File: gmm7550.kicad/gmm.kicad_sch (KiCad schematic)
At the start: 6 parts

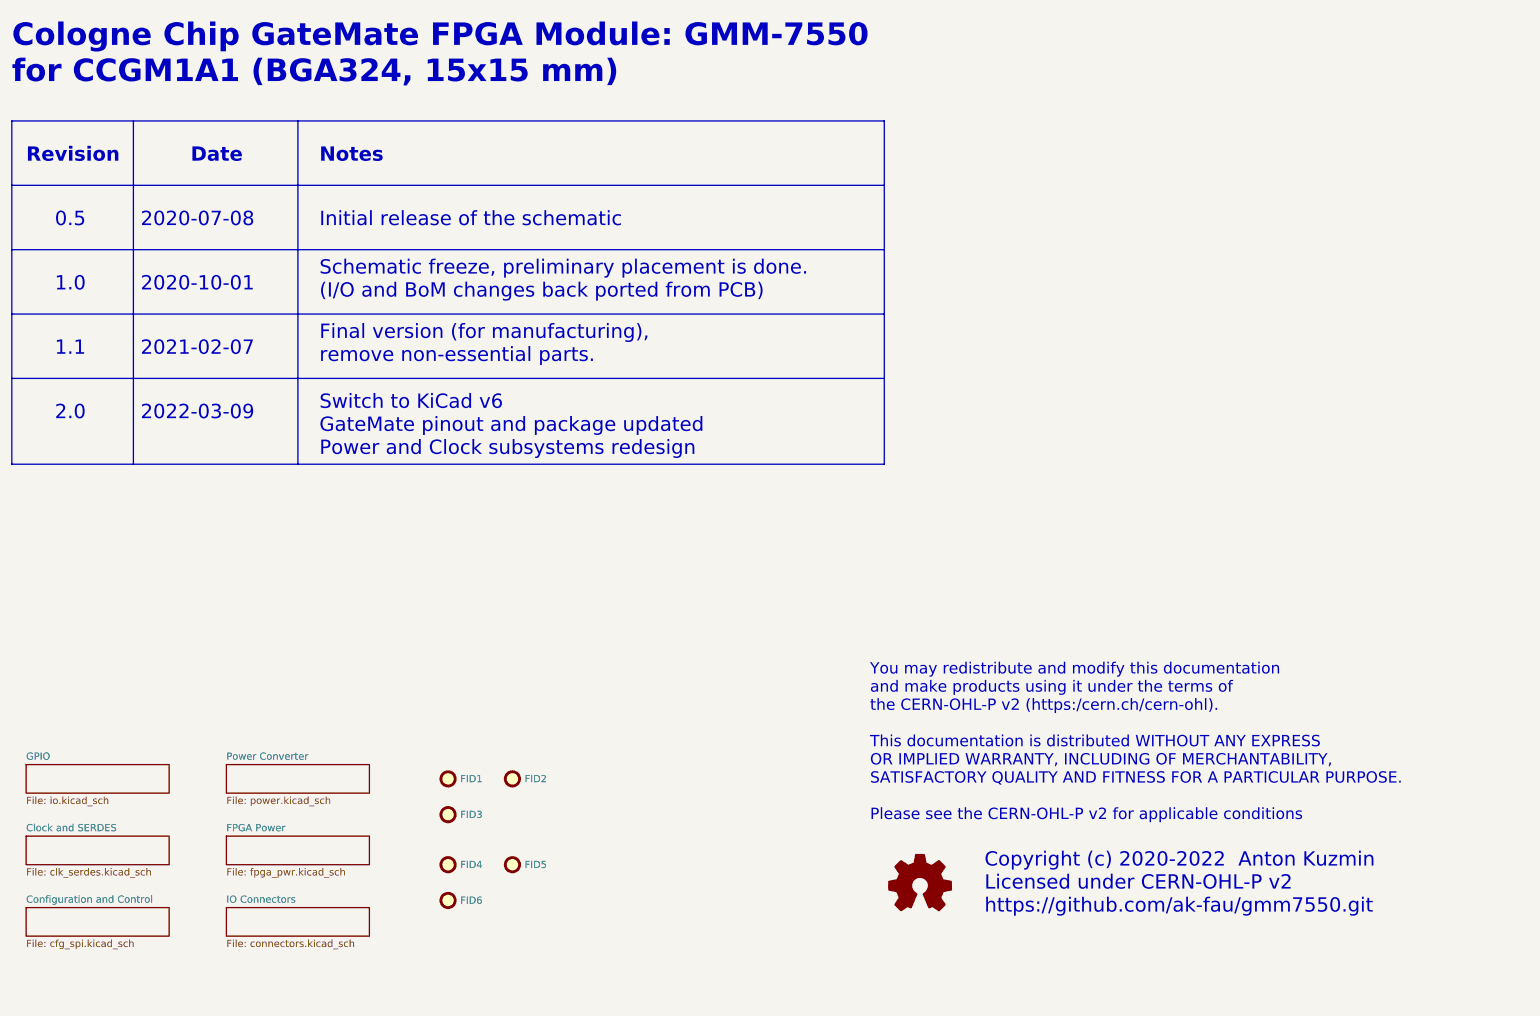
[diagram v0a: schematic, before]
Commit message: Change U7 footprint due to the part availability, revision and date are updated, DRC warnings clean-up (GMM-7550)
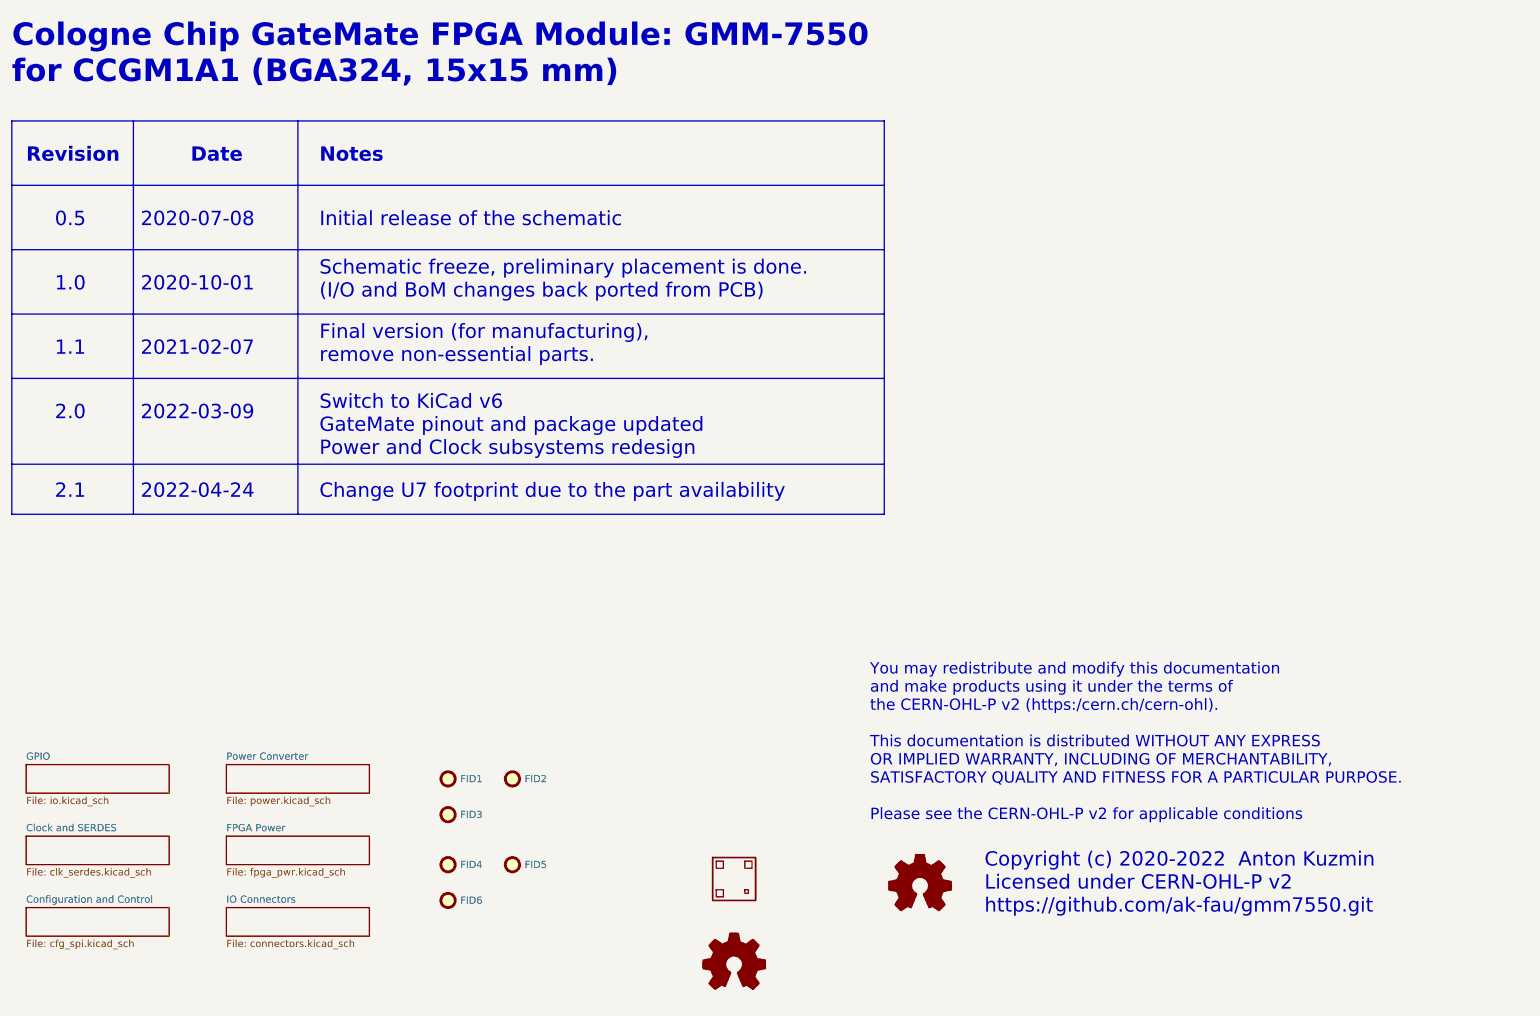
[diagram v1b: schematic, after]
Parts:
- added LOGO1: (no value), symbol Graphic:Logo_Open_Hardware_Small
- added QR1: (no value), gmm:GitHub_link_QR, symbol gmm_v6:GitHub_link_QR
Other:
- note added: "2.1"
- note added: "2022-04-24"
- note added: "Change U7 footprint due to the part availability"
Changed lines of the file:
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@@
   (title_block
     (title "GateMate FPGA Module: GMM-7550")
-    (date "2022-03-09")
-    (rev "2.0")
+    (date "2022-04-24")
+    (rev "2.1")
   )
   (polyline (pts (xy 25.4 72.39) (xy 180.34 72.39))
     (stroke (width 0.2032) (type solid) (color 0 0 0 0))
   )
+  (polyline (pts (xy 25.4 99.06) (xy 180.34 99.06))
+    (stroke (width 0.2032) (type solid) (color 0 0 0 0))
+  )
   (polyline (pts (xy 25.4 83.82) (xy 180.34 83.82))
     (stroke (width 0.2032) (type solid) (color 0 0 0 0))
   )
-  (polyline (pts (xy 180.34 38.1) (xy 180.34 99.06))
+  (polyline (pts (xy 180.34 38.1) (xy 180.34 107.95))
     (stroke (width 0.2032) (type solid) (color 0 0 0 0))
   )
-  (polyline (pts (xy 46.99 38.1) (xy 46.99 99.06))
+  (polyline (pts (xy 46.99 38.1) (xy 46.99 107.95))
     (stroke (width 0.2032) (type solid) (color 0 0 0 0))
   )
@@
     (stroke (width 0.2032) (type solid) (color 0 0 0 0))
   )
-  (polyline (pts (xy 76.2 38.1) (xy 76.2 99.06))
+  (polyline (pts (xy 76.2 38.1) (xy 76.2 107.95))
     (stroke (width 0.2032) (type solid) (color 0 0 0 0))
   )
@@
     (stroke (width 0.2032) (type solid) (color 0 0 0 0))
   )
-  (polyline (pts (xy 25.4 38.1) (xy 25.4 99.06))
+  (polyline (pts (xy 25.4 38.1) (xy 25.4 107.95))
     (stroke (width 0.2032) (type solid) (color 0 0 0 0))
   )
-  (polyline (pts (xy 25.4 99.06) (xy 180.34 99.06))
+  (polyline (pts (xy 25.4 107.95) (xy 180.34 107.95))
     (stroke (width 0.2032) (type solid) (color 0 0 0 0))
   )
@@
   (text "Final version (for manufacturing),\nremove non-essential parts."
     (at 80.01 81.28 0)
+    (effects (font (size 2.54 2.54)) (justify left bottom))
+  )
+  (text "2022-04-24" (at 48.26 105.41 0)
     (effects (font (size 2.54 2.54)) (justify left bottom))
   )
@@
     (effects (font (size 2.54 2.54)) (justify left bottom))
   )
+  (text "Change U7 footprint due to the part availability" (at 80.01 105.41 0)
+    (effects (font (size 2.54 2.54)) (justify left bottom))
+  )
   (text "Cologne Chip GateMate FPGA Module: GMM-7550\nfor CCGM1A1 (BGA324, 15x15 mm)"
     (at 25.4 31.75 0)
     (effects (font (size 3.9878 3.9878) (thickness 0.7976) bold) (justify left bottom))
+  )
+  (text "2.1" (at 33.02 105.41 0)
+    (effects (font (size 2.54 2.54)) (justify left bottom))
   )
   (text "2.0" (at 33.02 91.44 0)
@@
     )
     (property "Datasheet" "~" (id 3) (at 186.69 173.99 0)
+      (effects (font (size 1.27 1.27)) hide)
+    )
+  )
+  (symbol (lib_id "gmm_v6:GitHub_link_QR") (at 153.67 172.72 0) (unit 1)
+    (in_bom no) (on_board yes)
+    (property "Reference" "QR1" (id 0) (at 153.67 172.72 0)
+      (effects (font (size 1.27 1.27)) hide)
+    )
+    (property "Value" "" (id 1) (at 147.32 177.8 0)
+      (effects (font (size 1.27 1.27)) (justify left))
+    )
+    (property "Footprint" "gmm:GitHub_link_QR" (id 2) (at 153.67 172.72 0)
+      (effects (font (size 1.27 1.27)) hide)
+    )
+    (property "Datasheet" "" (id 3) (at 153.67 172.72 0)
+      (effects (font (size 1.27 1.27)) hide)
+    )
+  )
+  (symbol (lib_name "Logo_Open_Hardware_Small_1") (lib_id "Graphic:Logo_Open_Hardware_Small") (at 153.67 187.96 0) (unit 1)
+    (in_bom no) (on_board yes) (fields_autoplaced)
+    (property "Reference" "LOGO1" (id 0) (at 153.67 180.975 0)
+      (effects (font (size 1.27 1.27)) hide)
+    )
+    (property "Value" "" (id 1) (at 153.67 193.675 0))
+    (property "Footprint" "" (id 2) (at 153.67 187.96 0)
+      (effects (font (size 1.27 1.27)) hide)
+    )
+    (property "Datasheet" "~" (id 3) (at 153.67 187.96 0)
       (effects (font (size 1.27 1.27)) hide)
     )
@@
       (reference "L10") (unit 1) (value "ASPIAIG-FLR4020-1R0M-T") (footprint "gmm:L_Abracon_F4020_4.1x4.1mm")
     )
+    (path "/2df1f7fd-f252-4599-b779-f9b4ea84bccf"
+      (reference "LOGO1") (unit 1) (value "Logo_Open_Hardware_Small") (footprint "Symbol:OSHW-Logo2_7.3x6mm_SilkScreen")
+    )
     (path "/00000000-0000-0000-0000-00005fda34fc/00000000-0000-0000-0000-00006034eea1"
       (reference "MH1") (unit 1) (value "MountingHole_Pad") (footprint "MountingHole:MountingHole_3.2mm_M3_ISO7380_Pad")
@@
       (reference "Q1") (unit 1) (value "NX6008NBK") (footprint "Package_TO_SOT_SMD:SOT-23")
     )
+    (path "/110da1e9-fe95-4da1-a138-f5581271ace8"
+      (reference "QR1") (unit 1) (value "GitHub_link_QR") (footprint "gmm:GitHub_link_QR")
+    )
     (path "/00000000-0000-0000-0000-00005e836017/c7b3e4a6-2c9c-439f-a6b0-39536d50f535"
       (reference "R1") (unit 1) (value "33") (footprint "Resistor_SMD:R_0402_1005Metric")
@@
     )
     (path "/00000000-0000-0000-0000-00005e920ad5/00000000-0000-0000-0000-00005f2d851c"
-      (reference "U7") (unit 1) (value "74LVC1G07") (footprint "Package_TO_SOT_SMD:SOT-353_SC-70-5")
+      (reference "U7") (unit 1) (value "74LVC1G07") (footprint "Package_TO_SOT_SMD:SOT-23-5")
     )
     (path "/00000000-0000-0000-0000-00005e920ad5/00000000-0000-0000-0000-00005eb0cd7e"

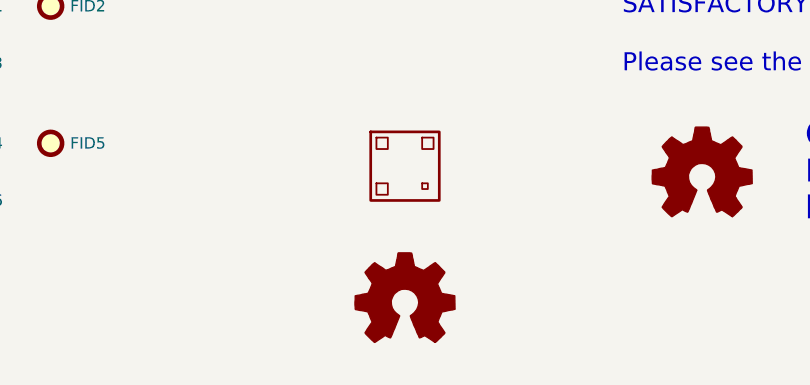
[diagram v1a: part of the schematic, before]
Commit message: Update designs to KiCad v7
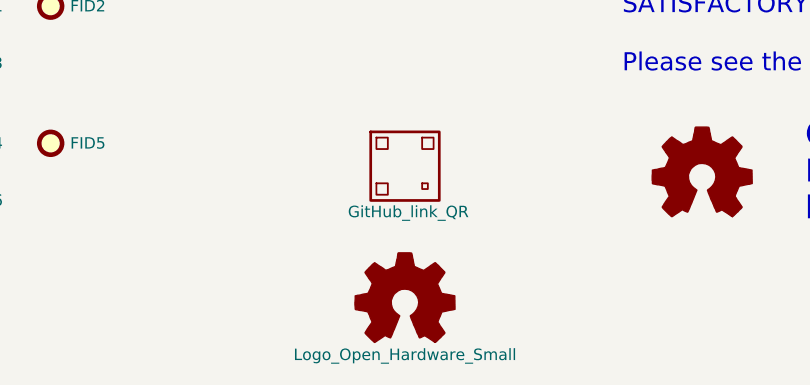
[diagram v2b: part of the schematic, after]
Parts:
- LOGO1: value (none) -> Logo_Open_Hardware_Small; footprint (none) -> Symbol:OSHW-Logo2_7.3x6mm_SilkScreen
- QR1: value (none) -> GitHub_link_QR

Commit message: Update copyright years and increment revision
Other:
- note added: "2.2"
- note added: "2024-01-27"
- note added: "Copyright (c) 2020-2024 Anton Kuzmin Licensed under CERN-OHL-P v2 https://github.com/gmm-7550/"
- note removed: "Copyright (c) 2020-2022 Anton Kuzmin Licensed under CERN-OHL-P v2 https://github.com/ak-fau/gmm7550.git"
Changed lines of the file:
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@@
   (title_block
     (title "GateMate FPGA Module: GMM-7550")
-    (date "2022-04-24")
-    (rev "2.1")
+    (date "2022-04-27")
+    (rev "2.2")
   )
   (polyline (pts (xy 25.4 72.39) (xy 180.34 72.39))
@@
     (stroke (width 0.2032) (type solid))
   )
-  (polyline (pts (xy 180.34 38.1) (xy 180.34 107.95))
+  (polyline (pts (xy 180.34 38.1) (xy 180.34 127))
     (stroke (width 0.2032) (type solid))
   )
-  (polyline (pts (xy 46.99 38.1) (xy 46.99 107.95))
+  (polyline (pts (xy 46.99 38.1) (xy 46.99 127))
     (stroke (width 0.2032) (type solid))
   )
@@
     (stroke (width 0.2032) (type solid))
   )
-  (polyline (pts (xy 76.2 38.1) (xy 76.2 107.95))
+  (polyline (pts (xy 76.2 38.1) (xy 76.2 127))
     (stroke (width 0.2032) (type solid))
   )
@@
     (stroke (width 0.2032) (type solid))
   )
-  (polyline (pts (xy 25.4 38.1) (xy 25.4 107.95))
+  (polyline (pts (xy 25.4 107.95) (xy 180.34 107.95))
     (stroke (width 0.2032) (type solid))
   )
-  (polyline (pts (xy 25.4 107.95) (xy 180.34 107.95))
+  (polyline (pts (xy 25.4 38.1) (xy 25.4 127))
+    (stroke (width 0.2032) (type solid))
+  )
+  (polyline (pts (xy 25.4 127) (xy 180.34 127))
     (stroke (width 0.2032) (type solid))
   )
@@
     (effects (font (size 2.54 2.54)) (justify left bottom))
   )
-  (text "Copyright (c) 2020-2022  Anton Kuzmin\nLicensed under CERN-OHL-P v2\nhttps://github.com/ak-fau/gmm7550.git"
+  (text "Copyright (c) 2020-2024  Anton Kuzmin\nLicensed under CERN-OHL-P v2\nhttps://github.com/gmm-7550/"
     (at 198.12 179.07 0)
     (effects (font (size 2.54 2.54)) (justify left bottom))
@@
   (text "Switch to KiCad v6\nGateMate pinout and package updated\nPower and Clock subsystems redesign\n"
     (at 80.01 97.79 0)
+    (effects (font (size 2.54 2.54)) (justify left bottom))
+  )
+  (text "2.2" (at 33.02 114.935 0)
     (effects (font (size 2.54 2.54)) (justify left bottom))
   )
@@
     (effects (font (size 2.54 2.54)) (justify left bottom))
   )
+  (text "2024-01-27" (at 48.26 114.935 0)
+    (effects (font (size 2.54 2.54)) (justify left bottom))
+  )
